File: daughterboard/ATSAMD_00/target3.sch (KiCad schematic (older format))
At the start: 0 parts

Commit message: further work on ATSAMD daughterboard
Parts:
- added C?: 10u, symbol Device:C_Small
- added C?: 1u, symbol Device:C_Small
- added C? (x3): 100n, symbol Device:C_Small
- added JP?: NRST, symbol Jumper:SolderJumper_2_Open
- added R?: 10k, symbol Device:R_Small
- added R?: 330, symbol Device:R_Small
- added R?: 1k, symbol Device:R_Small
- added R? (x2): 100k, symbol Device:R_Small
- added U?: ATSAMD21E16L-AFT, hive_daughterboard:ATSAMD21E16L-AFT, symbol hive_daughterboard:ATSAMD21E16L-AFT
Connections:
- net +3V3: now also C?.1, C?.1, C?.1, R?.2, R?.2, U?.28 (VDDIO), U?.9 (VDDIO/ANA)
- net GPIO3.0: now also U?.17 (PA16)
- net GPIO3.1: now also U?.18 (PA17)
- net GPIO3.2: now also U?.19 (PA18)
- net GPIO3.3: now also U?.20 (PA19)
- net RST_3: now also C?.1, R?.1, R?.2, U?.25 (~RESET~)
- net TCK|SWDCLK_3: now also R?.1, U?.29 (PA30)
- net TDI|NC_3: now also R?.1
- net TDO|SWO_3: now also R?.1
- net TMS|SWDIO_3: now also U?.30 (PA31)
- net UART_RxD3: now also U?.11 (PA08)
- net UART_TxD3: now also U?.13 (PA10)
- new net: C?.1, U?.27 (VDDCORE)
- new net: JP?.2 (B), R?.1
- new net GND: C?.2, C?.2, C?.2, C?.2, C?.2, JP?.1 (A), R?.2, R?.2, U?.10 (GND), U?.26 (GND)
- no-connect marks 0 -> 18
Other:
- note removed: "Power"

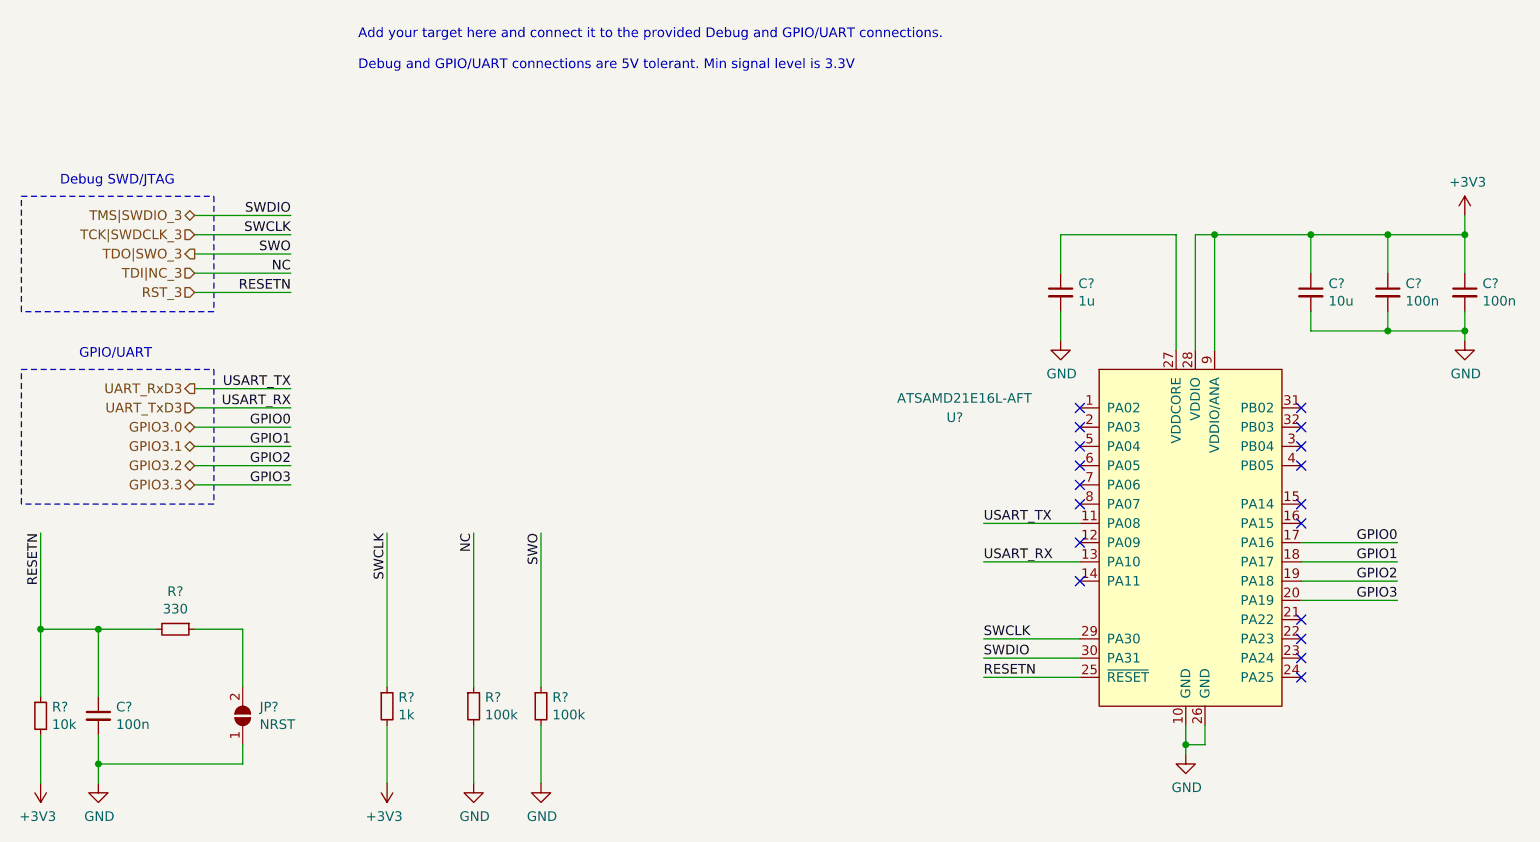
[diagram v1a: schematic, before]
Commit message: ERC on daughterboards
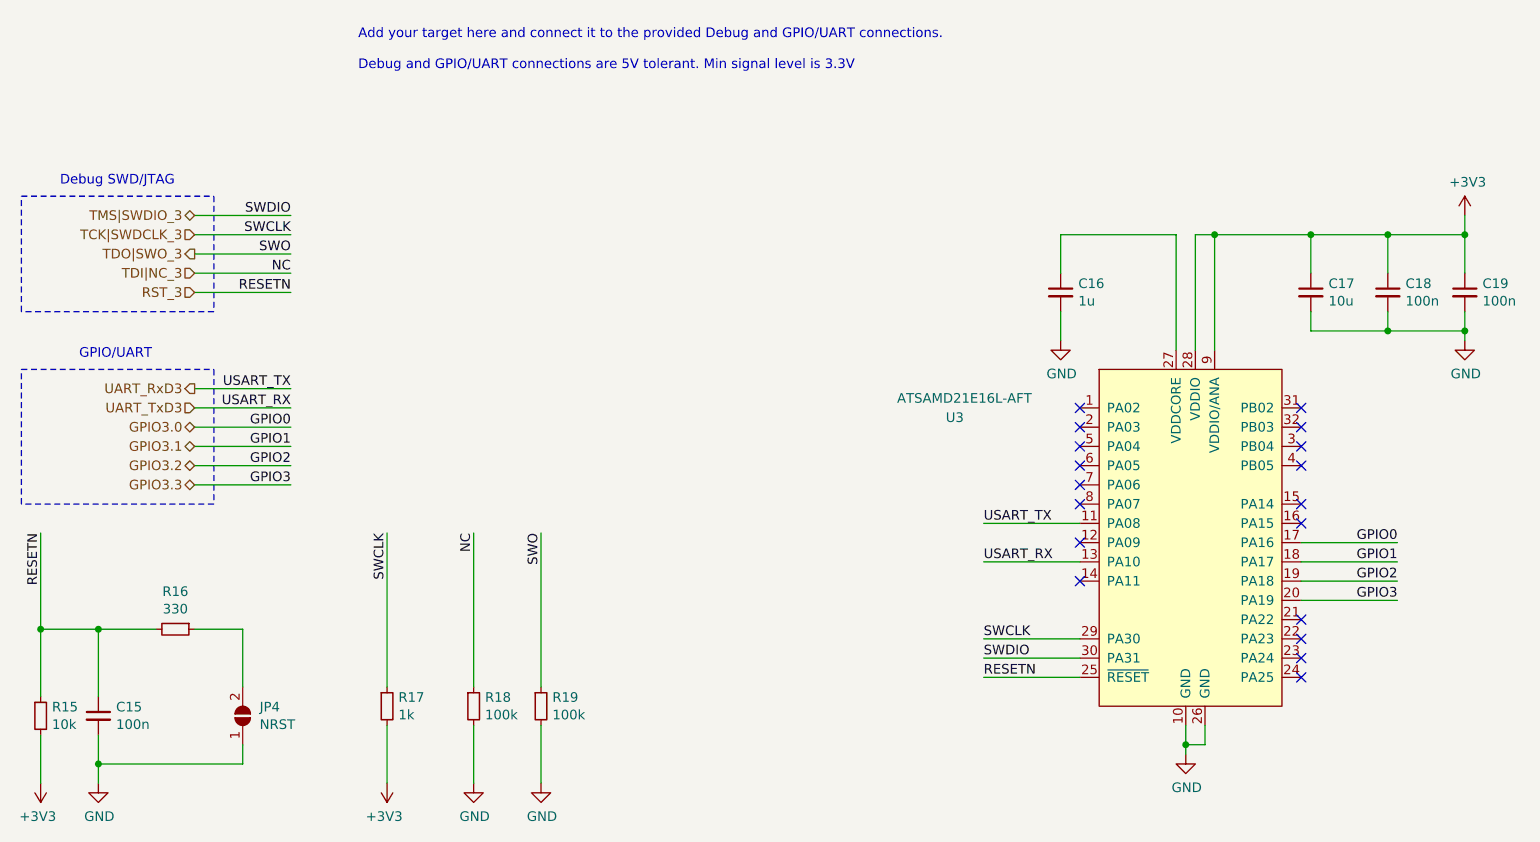
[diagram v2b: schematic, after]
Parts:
- gave numbers to parts that had none: 12
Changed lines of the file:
@@
 Add your target here and connect it to the provided Debug and GPIO/UART connections.\n\nDebug and GPIO/UART connections are 5V tolerant. Min signal level is 3.3V
 $Comp
-L hive_daughterboard:ATSAMD21E16L-AFT U?
+L hive_daughterboard:ATSAMD21E16L-AFT U3
 U 1 1 618B5040
 P 6850 2500
-F 0 "U?" H 5600 2250 50  0000 C CNN
+F 0 "U3" H 5600 2250 50  0000 C CNN
 F 1 "ATSAMD21E16L-AFT" H 5650 2350 50  0000 C CNN
 F 2 "hive_daughterboard:ATSAMD21E16L-AFT" H 6850 2500 50  0001 C CNN
@@
 P 7450 2100
 AR Path="/616688D6/618BD711" Ref="C?"  Part="1"
-AR Path="/61668157/618BD711" Ref="C?"  Part="1"
-F 0 "C?" H 7542 2146 50  0000 L CNN
+AR Path="/61668157/618BD711" Ref="C17"  Part="1"
+F 0 "C17" H 7542 2146 50  0000 L CNN
 F 1 "10u" H 7542 2055 50  0000 L CNN
 F 2 "" H 7450 2100 50  0001 C CNN
@@
 P 6150 2100
 AR Path="/616688D6/618BD717" Ref="C?"  Part="1"
-AR Path="/61668157/618BD717" Ref="C?"  Part="1"
-F 0 "C?" H 6242 2146 50  0000 L CNN
+AR Path="/61668157/618BD717" Ref="C16"  Part="1"
+F 0 "C16" H 6242 2146 50  0000 L CNN
 F 1 "1u" H 6242 2055 50  0000 L CNN
 F 2 "" H 6150 2100 50  0001 C CNN
@@
 P 7850 2100
 AR Path="/616688D6/618BD729" Ref="C?"  Part="1"
-AR Path="/61668157/618BD729" Ref="C?"  Part="1"
-F 0 "C?" H 7942 2146 50  0000 L CNN
+AR Path="/61668157/618BD729" Ref="C18"  Part="1"
+F 0 "C18" H 7942 2146 50  0000 L CNN
 F 1 "100n" H 7942 2055 50  0000 L CNN
 F 2 "" H 7850 2100 50  0001 C CNN
@@
 P 8250 2100
 AR Path="/616688D6/618BD72F" Ref="C?"  Part="1"
-AR Path="/61668157/618BD72F" Ref="C?"  Part="1"
-F 0 "C?" H 8342 2146 50  0000 L CNN
+AR Path="/61668157/618BD72F" Ref="C19"  Part="1"
+F 0 "C19" H 8342 2146 50  0000 L CNN
 F 1 "100n" H 8342 2055 50  0000 L CNN
 F 2 "" H 8250 2100 50  0001 C CNN
@@
 P 6150 2350
 AR Path="/616688D6/618BD73B" Ref="#PWR?"  Part="1"
-AR Path="/61668157/618BD73B" Ref="#PWR?"  Part="1"
-F 0 "#PWR?" H 6150 2100 50  0001 C CNN
+AR Path="/61668157/618BD73B" Ref="#PWR0140"  Part="1"
+F 0 "#PWR0140" H 6150 2100 50  0001 C CNN
 F 1 "GND" H 6155 2177 50  0000 C CNN
 F 2 "" H 6150 2350 50  0001 C CNN
@@
 P 8250 2350
 AR Path="/616688D6/618BD767" Ref="#PWR?"  Part="1"
-AR Path="/61668157/618BD767" Ref="#PWR?"  Part="1"
-F 0 "#PWR?" H 8250 2100 50  0001 C CNN
+AR Path="/61668157/618BD767" Ref="#PWR0141"  Part="1"
+F 0 "#PWR0141" H 8250 2100 50  0001 C CNN
 F 1 "GND" H 8255 2177 50  0000 C CNN
 F 2 "" H 8250 2350 50  0001 C CNN
@@
 P 8250 1700
 AR Path="/616688D6/618BD77B" Ref="#PWR?"  Part="1"
-AR Path="/61668157/618BD77B" Ref="#PWR?"  Part="1"
-F 0 "#PWR?" H 8250 1550 50  0001 C CNN
+AR Path="/61668157/618BD77B" Ref="#PWR0142"  Part="1"
+F 0 "#PWR0142" H 8250 1550 50  0001 C CNN
 F 1 "+3V3" H 8265 1873 50  0000 C CNN
 F 2 "" H 8250 1700 50  0001 C CNN
@@
 RESETN
 $Comp
-L Device:R_Small R?
+L Device:R_Small R15
 U 1 1 618D0C5E
 P 850 4300
-F 0 "R?" H 909 4346 50  0000 L CNN
+F 0 "R15" H 909 4346 50  0000 L CNN
 F 1 "10k" H 909 4255 50  0000 L CNN
 F 2 "" H 850 4300 50  0001 C CNN
@@
 $EndComp
 $Comp
-L Device:R_Small R?
+L Device:R_Small R16
 U 1 1 618D0C64
 P 1550 3850
-F 0 "R?" V 1354 3850 50  0000 C CNN
+F 0 "R16" V 1354 3850 50  0000 C CNN
 F 1 "330" V 1445 3850 50  0000 C CNN
 F 2 "" H 1550 3850 50  0001 C CNN
@@
 $EndComp
 $Comp
-L Device:C_Small C?
+L Device:C_Small C15
 U 1 1 618D0C6A
 P 1150 4300
-F 0 "C?" H 1242 4346 50  0000 L CNN
+F 0 "C15" H 1242 4346 50  0000 L CNN
 F 1 "100n" H 1242 4255 50  0000 L CNN
 F 2 "" H 1150 4300 50  0001 C CNN
@@
 $EndComp
 $Comp
-L power:+3V3 #PWR?
+L power:+3V3 #PWR0143
 U 1 1 618D0C70
 P 850 4650
-F 0 "#PWR?" H 850 4500 50  0001 C CNN
+F 0 "#PWR0143" H 850 4500 50  0001 C CNN
 F 1 "+3V3" H 865 4823 50  0000 C CNN
 F 2 "" H 850 4650 50  0001 C CNN
@@
 	1150 3850 850  3850
 $Comp
-L power:GND #PWR?
+L power:GND #PWR0144
 U 1 1 618D0C7E
 P 1150 4650
-F 0 "#PWR?" H 1150 4400 50  0001 C CNN
+F 0 "#PWR0144" H 1150 4400 50  0001 C CNN
 F 1 "GND" H 1155 4477 50  0000 C CNN
 F 2 "" H 1150 4650 50  0001 C CNN
@@
 	1150 4650 1150 4550
 $Comp
-L Jumper:SolderJumper_2_Open JP?
+L Jumper:SolderJumper_2_Open JP4
 U 1 1 618D0C85
 P 1900 4300
-F 0 "JP?" V 1946 4212 50  0000 R CNN
+F 0 "JP4" V 1946 4212 50  0000 R CNN
 F 1 "NRST" V 1855 4212 50  0000 R CNN
 F 2 "" H 1900 4300 50  0001 C CNN
@@
 SWCLK
 $Comp
-L Device:R_Small R?
+L Device:R_Small R17
 U 1 1 618D0C92
 P 2650 4250
-F 0 "R?" H 2709 4296 50  0000 L CNN
+F 0 "R17" H 2709 4296 50  0000 L CNN
 F 1 "1k" H 2709 4205 50  0000 L CNN
 F 2 "" H 2650 4250 50  0001 C CNN
@@
 $EndComp
 $Comp
-L power:+3V3 #PWR?
+L power:+3V3 #PWR0145
 U 1 1 618D0C98
 P 2650 4650
-F 0 "#PWR?" H 2650 4500 50  0001 C CNN
+F 0 "#PWR0145" H 2650 4500 50  0001 C CNN
 F 1 "+3V3" H 2665 4823 50  0000 C CNN
 F 2 "" H 2650 4650 50  0001 C CNN
@@
 NC
 $Comp
-L Device:R_Small R?
+L Device:R_Small R18
 U 1 1 618D0CA1
 P 3100 4250
-F 0 "R?" H 3159 4296 50  0000 L CNN
+F 0 "R18" H 3159 4296 50  0000 L CNN
 F 1 "100k" H 3159 4205 50  0000 L CNN
 F 2 "" H 3100 4250 50  0001 C CNN
@@
 $EndComp
 $Comp
-L power:GND #PWR?
+L power:GND #PWR0146
 U 1 1 618D0CA7
 P 3100 4650
-F 0 "#PWR?" H 3100 4400 50  0001 C CNN
+F 0 "#PWR0146" H 3100 4400 50  0001 C CNN
 F 1 "GND" H 3105 4477 50  0000 C CNN
 F 2 "" H 3100 4650 50  0001 C CNN
@@
 SWO
 $Comp
-L Device:R_Small R?
+L Device:R_Small R19
 U 1 1 618D3D91
 P 3450 4250
-F 0 "R?" H 3509 4296 50  0000 L CNN
+F 0 "R19" H 3509 4296 50  0000 L CNN
 F 1 "100k" H 3509 4205 50  0000 L CNN
 F 2 "" H 3450 4250 50  0001 C CNN
@@
 $EndComp
 $Comp
-L power:GND #PWR?
+L power:GND #PWR0147
 U 1 1 618D3D97
 P 3450 4650
-F 0 "#PWR?" H 3450 4400 50  0001 C CNN
+F 0 "#PWR0147" H 3450 4400 50  0001 C CNN
 F 1 "GND" H 3455 4477 50  0000 C CNN
 F 2 "" H 3450 4650 50  0001 C CNN
@@
 P 6800 4500
 AR Path="/616688D6/618E8888" Ref="#PWR?"  Part="1"
-AR Path="/61668157/618E8888" Ref="#PWR?"  Part="1"
-F 0 "#PWR?" H 6800 4250 50  0001 C CNN
+AR Path="/61668157/618E8888" Ref="#PWR0148"  Part="1"
+F 0 "#PWR0148" H 6800 4250 50  0001 C CNN
 F 1 "GND" H 6805 4327 50  0000 C CNN
 F 2 "" H 6800 4500 50  0001 C CNN

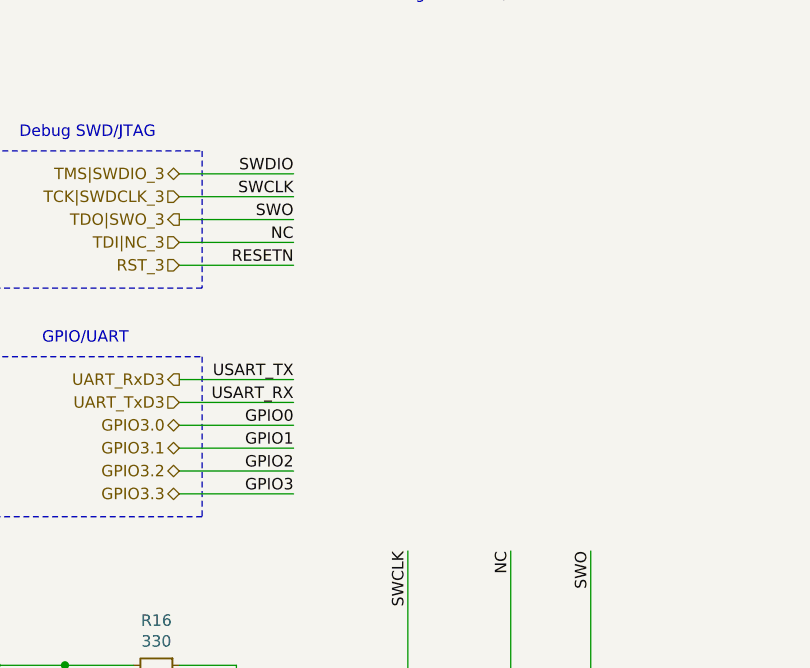
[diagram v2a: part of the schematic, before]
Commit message: added testpoints to daughterboards, updated readme
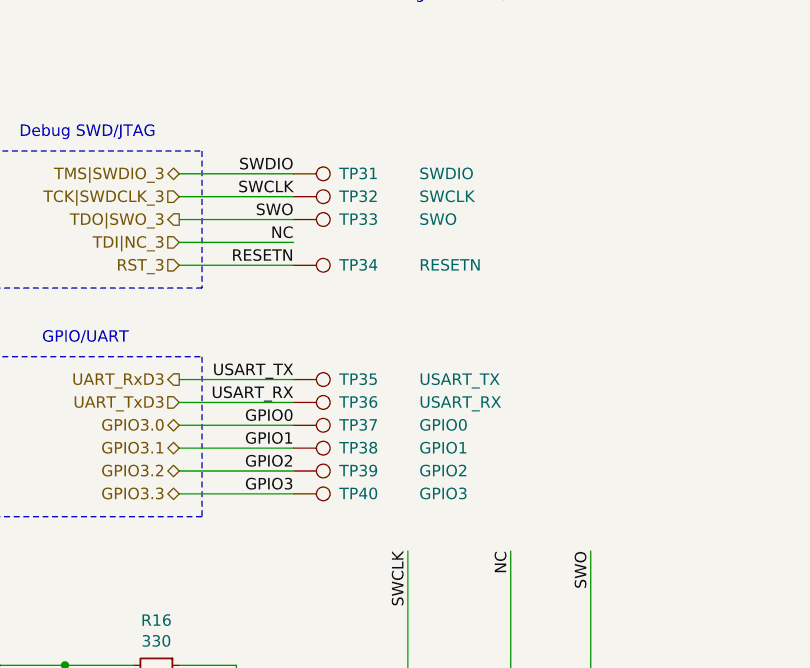
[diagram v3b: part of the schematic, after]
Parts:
- added TP31: SWDIO, symbol Connector:TestPoint
- added TP32: SWCLK, symbol Connector:TestPoint
- added TP33: SWO, symbol Connector:TestPoint
- added TP34: RESETN, symbol Connector:TestPoint
- added TP35: USART_TX, symbol Connector:TestPoint
- added TP36: USART_RX, symbol Connector:TestPoint
- added TP37: GPIO0, symbol Connector:TestPoint
- added TP38: GPIO1, symbol Connector:TestPoint
- added TP39: GPIO2, symbol Connector:TestPoint
- added TP40: GPIO3, symbol Connector:TestPoint
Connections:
- net GPIO3.0: now also TP37.1
- net GPIO3.1: now also TP38.1
- net GPIO3.2: now also TP39.1
- net GPIO3.3: now also TP40.1
- net RST_3: now also TP34.1
- net TCK|SWDCLK_3: now also TP32.1
- net TDO|SWO_3: now also TP33.1
- net TMS|SWDIO_3: now also TP31.1
- net UART_RxD3: now also TP35.1
- net UART_TxD3: now also TP36.1
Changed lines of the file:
@@
 Wire Wire Line
 	6800 4450 6800 4350
+$Comp
+L Connector:TestPoint TP?
+U 1 1 6191E7CC
+P 2150 1700
+AR Path="/616688D6/6191E7CC" Ref="TP?"  Part="1"
+AR Path="/61668157/6191E7CC" Ref="TP31"  Part="1"
+F 0 "TP31" V 2150 1900 50  0000 L CNN
+F 1 "SWDIO" V 2150 2250 50  0000 L CNN
+F 2 "" H 2350 1700 50  0001 C CNN
+F 3 "~" H 2350 1700 50  0001 C CNN
+	1    2150 1700
+	0    1    1    0
+$EndComp
+$Comp
+L Connector:TestPoint TP?
+U 1 1 6191E7D2
+P 2150 1800
+AR Path="/616688D6/6191E7D2" Ref="TP?"  Part="1"
+AR Path="/61668157/6191E7D2" Ref="TP32"  Part="1"
+F 0 "TP32" V 2150 2000 50  0000 L CNN
+F 1 "SWCLK" V 2150 2350 50  0000 L CNN
+F 2 "" H 2350 1800 50  0001 C CNN
+F 3 "~" H 2350 1800 50  0001 C CNN
+	1    2150 1800
+	0    1    1    0
+$EndComp
+$Comp
+L Connector:TestPoint TP?
+U 1 1 6191E7D8
+P 2150 1900
+AR Path="/616688D6/6191E7D8" Ref="TP?"  Part="1"
+AR Path="/61668157/6191E7D8" Ref="TP33"  Part="1"
+F 0 "TP33" V 2150 2100 50  0000 L CNN
+F 1 "SWO" V 2150 2450 50  0000 L CNN
+F 2 "" H 2350 1900 50  0001 C CNN
+F 3 "~" H 2350 1900 50  0001 C CNN
+	1    2150 1900
+	0    1    1    0
+$EndComp
+$Comp
+L Connector:TestPoint TP?
+U 1 1 6191E7DE
+P 2150 2100
+AR Path="/616688D6/6191E7DE" Ref="TP?"  Part="1"
+AR Path="/61668157/6191E7DE" Ref="TP34"  Part="1"
+F 0 "TP34" V 2150 2300 50  0000 L CNN
+F 1 "RESETN" V 2150 2650 50  0000 L CNN
+F 2 "" H 2350 2100 50  0001 C CNN
+F 3 "~" H 2350 2100 50  0001 C CNN
+	1    2150 2100
+	0    1    1    0
+$EndComp
+$Comp
+L Connector:TestPoint TP?
+U 1 1 6191E7E4
+P 2150 2600
+AR Path="/616688D6/6191E7E4" Ref="TP?"  Part="1"
+AR Path="/61668157/6191E7E4" Ref="TP35"  Part="1"
+F 0 "TP35" V 2150 2800 50  0000 L CNN
+F 1 "USART_TX" V 2150 3150 50  0000 L CNN
+F 2 "" H 2350 2600 50  0001 C CNN
+F 3 "~" H 2350 2600 50  0001 C CNN
+	1    2150 2600
+	0    1    -1   0
+$EndComp
+$Comp
+L Connector:TestPoint TP?
+U 1 1 6191E7EA
+P 2150 2700
+AR Path="/616688D6/6191E7EA" Ref="TP?"  Part="1"
+AR Path="/61668157/6191E7EA" Ref="TP36"  Part="1"
+F 0 "TP36" V 2150 2900 50  0000 L CNN
+F 1 "USART_RX" V 2150 3250 50  0000 L CNN
+F 2 "" H 2350 2700 50  0001 C CNN
+F 3 "~" H 2350 2700 50  0001 C CNN
+	1    2150 2700
+	0    1    -1   0
+$EndComp
+$Comp
+L Connector:TestPoint TP?
+U 1 1 6191E7F0
+P 2150 2800
+AR Path="/616688D6/6191E7F0" Ref="TP?"  Part="1"
+AR Path="/61668157/6191E7F0" Ref="TP37"  Part="1"
+F 0 "TP37" V 2150 3000 50  0000 L CNN
+F 1 "GPIO0" V 2150 3350 50  0000 L CNN
+F 2 "" H 2350 2800 50  0001 C CNN
+F 3 "~" H 2350 2800 50  0001 C CNN
+	1    2150 2800
+	0    1    -1   0
+$EndComp
+$Comp
+L Connector:TestPoint TP?
+U 1 1 6191E7F6
+P 2150 2900
+AR Path="/616688D6/6191E7F6" Ref="TP?"  Part="1"
+AR Path="/61668157/6191E7F6" Ref="TP38"  Part="1"
+F 0 "TP38" V 2150 3100 50  0000 L CNN
+F 1 "GPIO1" V 2150 3450 50  0000 L CNN
+F 2 "" H 2350 2900 50  0001 C CNN
+F 3 "~" H 2350 2900 50  0001 C CNN
+	1    2150 2900
+	0    1    -1   0
+$EndComp
+$Comp
+L Connector:TestPoint TP?
+U 1 1 6191E7FC
+P 2150 3000
+AR Path="/616688D6/6191E7FC" Ref="TP?"  Part="1"
+AR Path="/61668157/6191E7FC" Ref="TP39"  Part="1"
+F 0 "TP39" V 2150 3200 50  0000 L CNN
+F 1 "GPIO2" V 2150 3550 50  0000 L CNN
+F 2 "" H 2350 3000 50  0001 C CNN
+F 3 "~" H 2350 3000 50  0001 C CNN
+	1    2150 3000
+	0    1    -1   0
+$EndComp
+$Comp
+L Connector:TestPoint TP?
+U 1 1 6191E802
+P 2150 3100
+AR Path="/616688D6/6191E802" Ref="TP?"  Part="1"
+AR Path="/61668157/6191E802" Ref="TP40"  Part="1"
+F 0 "TP40" V 2150 3300 50  0000 L CNN
+F 1 "GPIO3" V 2150 3650 50  0000 L CNN
+F 2 "" H 2350 3100 50  0001 C CNN
+F 3 "~" H 2350 3100 50  0001 C CNN
+	1    2150 3100
+	0    1    -1   0
+$EndComp
 $EndSCHEMATC
